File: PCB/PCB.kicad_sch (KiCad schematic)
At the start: 0 parts

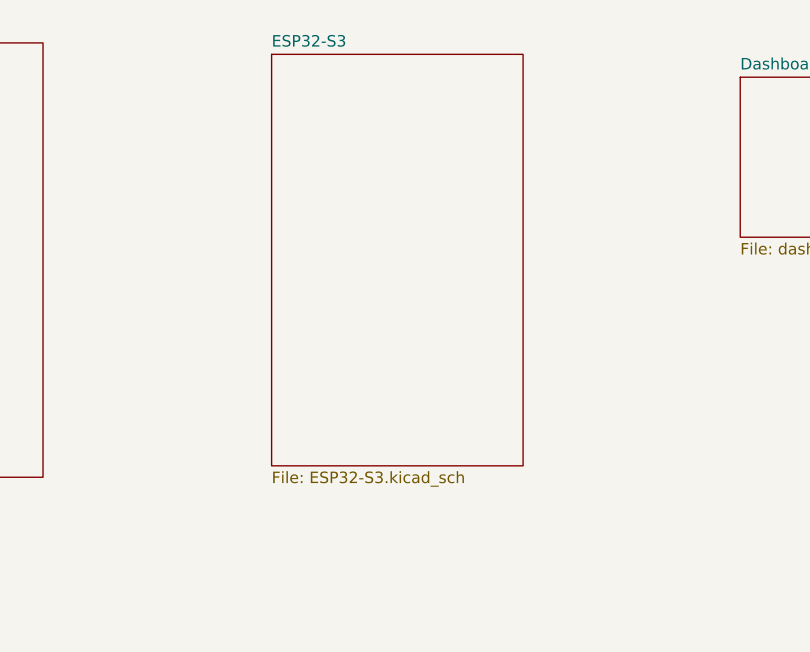
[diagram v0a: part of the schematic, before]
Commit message: [Schem] Added sensors connectors & finished Step down circuit
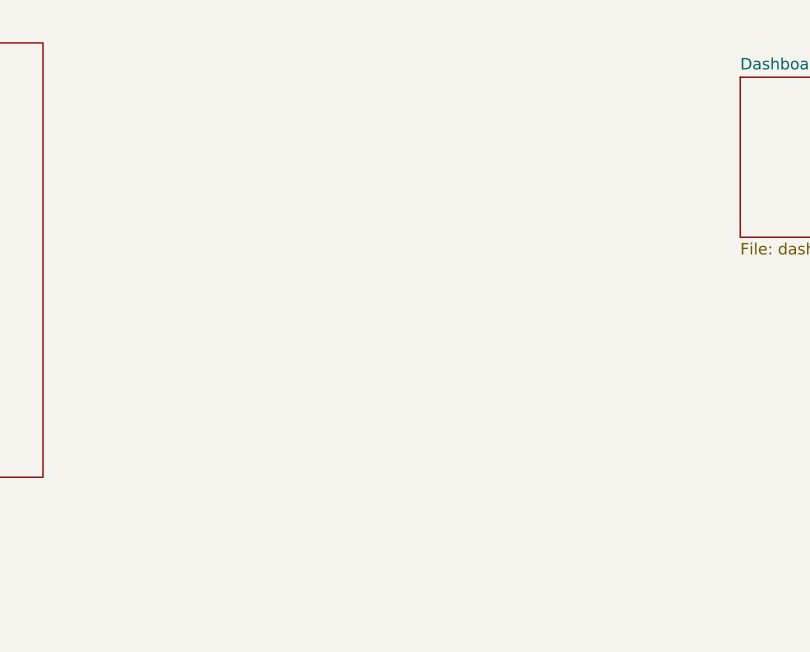
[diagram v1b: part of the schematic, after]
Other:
- removed sheet ESP32-S3
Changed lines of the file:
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@@
-	)
-	(sheet
-		(at 191.77 19.05)
-		(size 27.94 45.72)
-		(exclude_from_sim no)
-		(in_bom yes)
-		(on_board yes)
-		(dnp no)
-		(fields_autoplaced yes)
-		(stroke
-			(width 0.1524)
-			(type solid)
-		)
-		(fill
-			(color 0 0 0 0)
-		)
-		(property "Sheetname" "ESP32-S3"
-			(at 191.77 18.3384 0)
-			(show_name no)
-			(do_not_autoplace no)
-			(effects
-				(font
-					(size 1.27 1.27)
-				)
-				(justify left bottom)
-			)
-		)
-		(property "Sheetfile" "ESP32-S3.kicad_sch"
-			(at 191.77 65.3546 0)
-			(show_name no)
-			(do_not_autoplace no)
-			(effects
-				(font
-					(size 1.27 1.27)
-				)
-				(justify left top)
-			)
-		)
-		(instances
-			(project "PCB"
-				(path "/ce714510-8789-438c-9780-97c7c26e78af"
-					(page "3")
-				)
-			)
-		)
 	)
 	(sheet

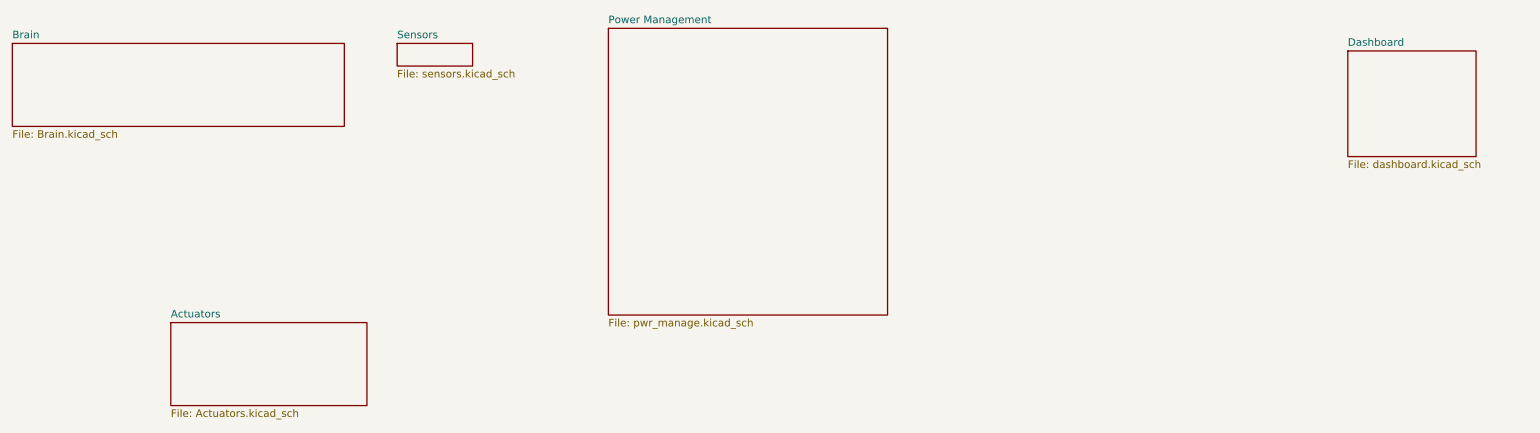
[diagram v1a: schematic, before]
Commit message: [Schem] Finished the Hierarchy Labels of all the pages
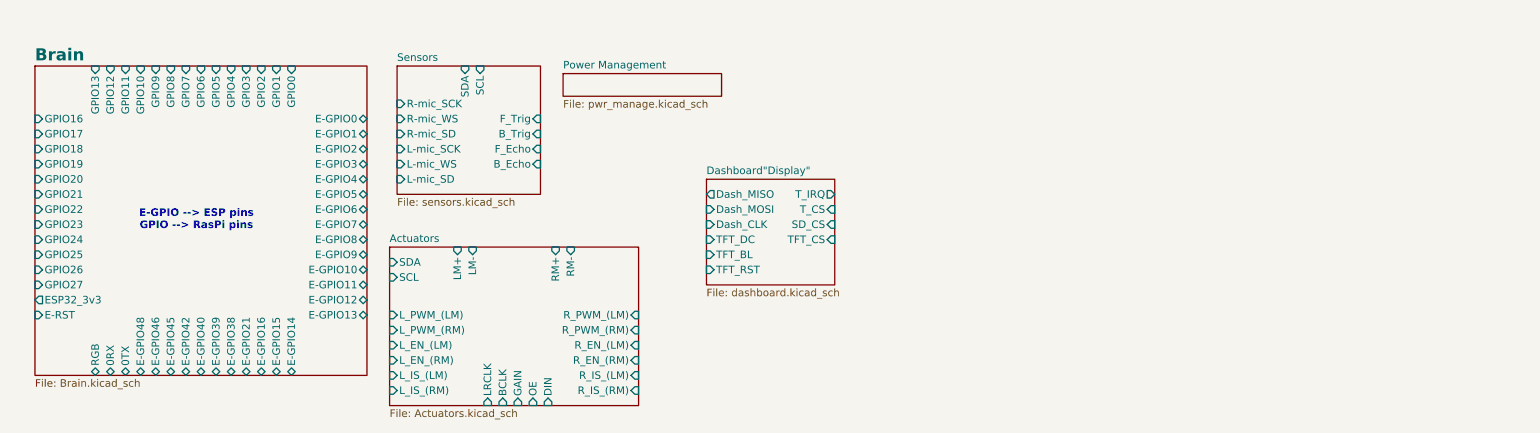
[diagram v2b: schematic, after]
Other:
- sheet Dashboard renamed Dashboard"Display"
- sheet Actuators ports: added BCLK, DIN, GAIN, LM+, LM-, LRCLK, L_EN_(LM), L_EN_(RM), L_IS_(LM), L_IS_(RM), L_PWM_(LM), L_PWM_(RM), OE, RM+, RM-, R_EN_(LM), R_EN_(RM), R_IS_(LM), R_IS_(RM), R_PWM_(LM), R_PWM_(RM), SCL, SDA; removed none
- sheet Brain ports: added 0RX, 0TX, E-GPIO0, E-GPIO1, E-GPIO10, E-GPIO11, E-GPIO12, E-GPIO13, E-GPIO14, E-GPIO15, E-GPIO16, E-GPIO2, E-GPIO21, E-GPIO3, E-GPIO38, E-GPIO39, E-GPIO4, E-GPIO40, E-GPIO42, E-GPIO45, E-GPIO46, E-GPIO48, E-GPIO5, E-GPIO6, E-GPIO7, E-GPIO8, E-GPIO9, E-RST, ESP32_3v3, GPIO0, GPIO1, GPIO10, GPIO11, GPIO12, GPIO13, GPIO16, GPIO17, GPIO18, GPIO19, GPIO2, GPIO20, GPIO21, GPIO22, GPIO23, GPIO24, GPIO25, GPIO26, GPIO27, GPIO3, GPIO4, GPIO5, GPIO6, GPIO7, GPIO8, GPIO9, RGB; removed none
- sheet Dashboard"Display" ports: added Dash_CLK, Dash_MISO, Dash_MOSI, SD_CS, TFT_BL, TFT_CS, TFT_DC, TFT_RST, T_CS, T_IRQ; removed none
- sheet Sensors ports: added B_Echo, B_Trig, F_Echo, F_Trig, L-mic_SCK, L-mic_SD, L-mic_WS, R-mic_SCK, R-mic_SD, R-mic_WS, SCL, SDA; removed none
- note added: "E-GPIO --> ESP pins GPIO --> RasPi pins"

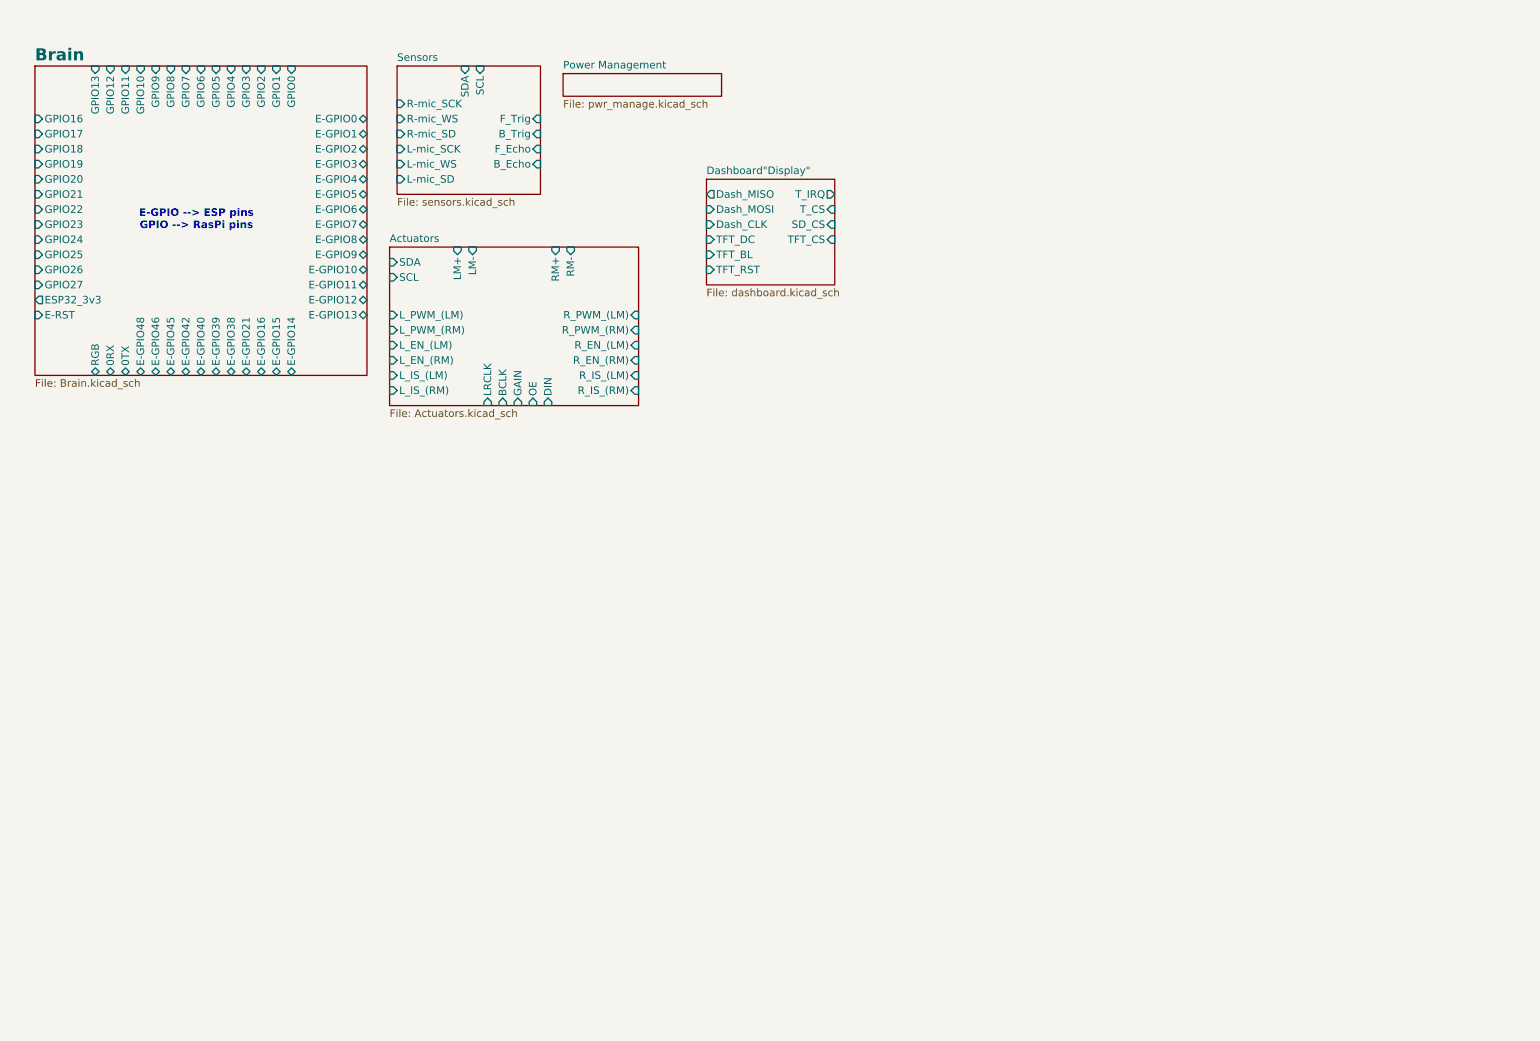
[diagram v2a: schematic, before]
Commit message: [Schem] Added all the net labels and connected the Dashboard screen
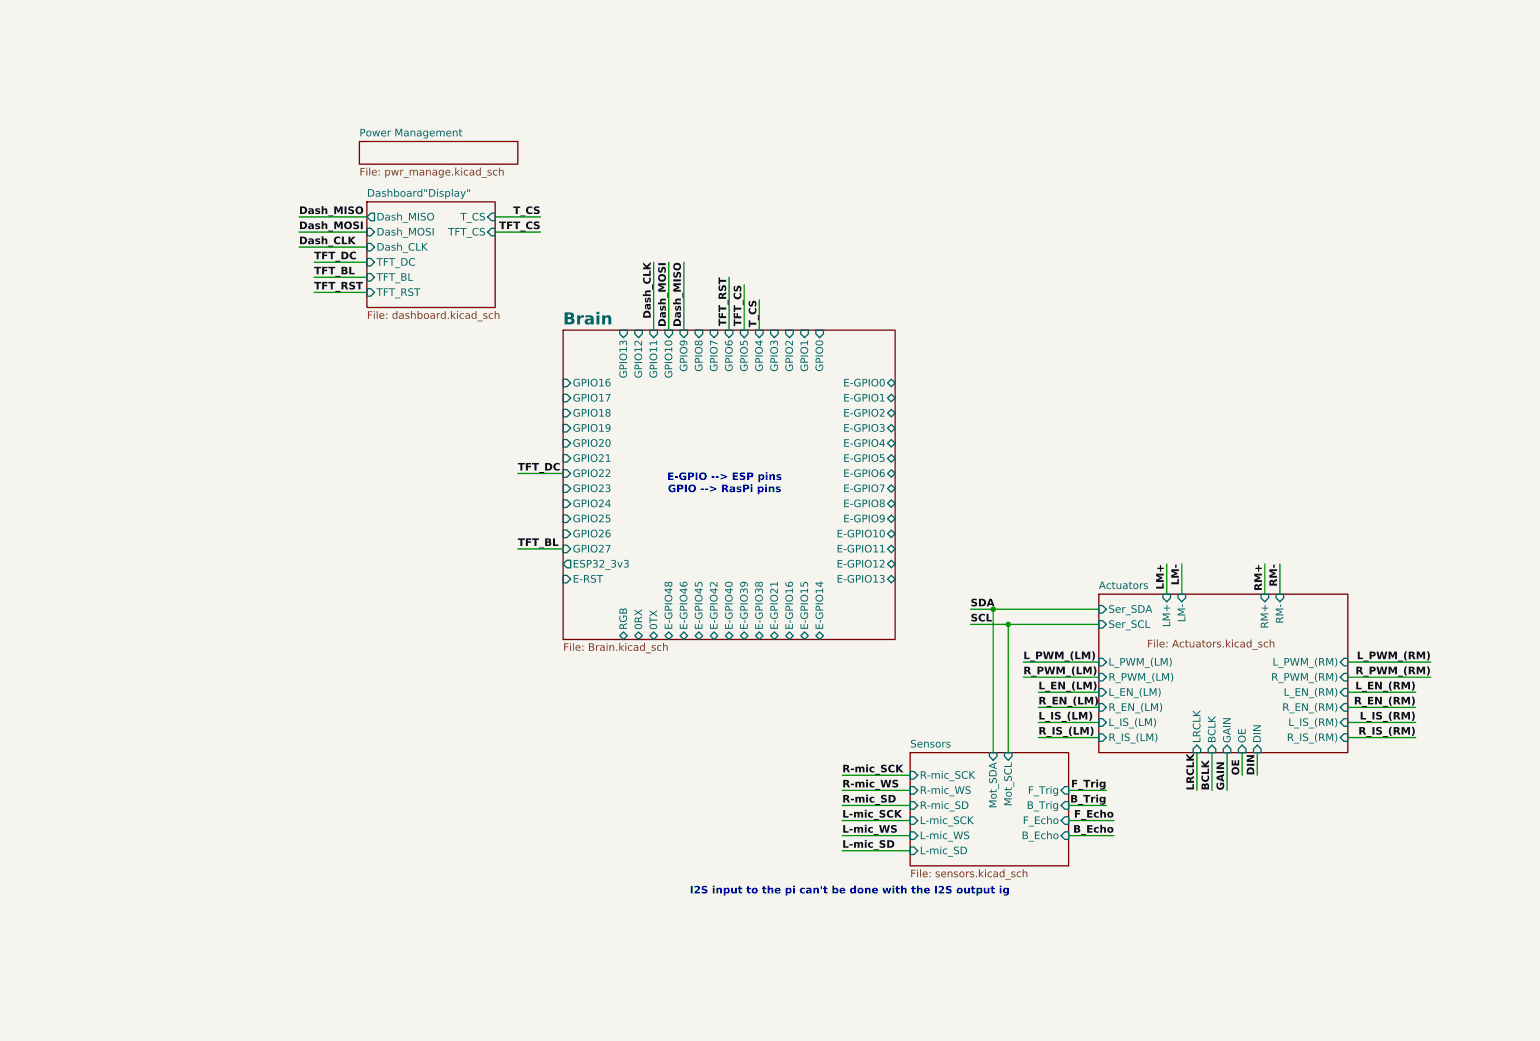
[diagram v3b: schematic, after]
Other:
- sheet Actuators ports: added Ser_SCL, Ser_SDA; removed SCL, SDA
- sheet Dashboard"Display" ports: added none; removed SD_CS, T_IRQ
- sheet Sensors ports: added Mot_SCL, Mot_SDA; removed SCL, SDA
- note added: "I2S input to the pi can't be done with the I2S output ig"

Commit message: [PCB] Assigned all the footprints
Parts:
- added J19: Free_GPIO, Connector_PinHeader_2.54mm:PinHeader_2x11_P2.54mm_Vertical, symbol Connector_Generic:Conn_02x11_Odd_Even
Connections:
- new net E-GPIO0: J19.8 (Pin_8)
- new net E-GPIO16: J19.12 (Pin_12)
- new net E-GPIO21: J19.14 (Pin_14)
- new net E-GPIO3: J19.10 (Pin_10)
- new net E-GPIO38: J19.16 (Pin_16)
- new net E-GPIO39: J19.18 (Pin_18)
- new net E-GPIO40: J19.20 (Pin_20)
- new net ESP32_3v3: J19.22 (Pin_22)
- new net GPIO0: J19.1 (Pin_1)
- new net GPIO1: J19.3 (Pin_3)
- new net GPIO12: J19.13 (Pin_13)
- new net GPIO13: J19.15 (Pin_15)
- new net GPIO16: J19.17 (Pin_17)
- new net GPIO17: J19.19 (Pin_19)
- new net GPIO2: J19.5 (Pin_5)
- new net GPIO23: J19.21 (Pin_21)
- new net GPIO24: J19.2 (Pin_2)
- new net GPIO25: J19.4 (Pin_4)
- new net GPIO26: J19.6 (Pin_6)
- new net GPIO3: J19.7 (Pin_7)
- new net GPIO7: J19.9 (Pin_9)
- new net GPIO8: J19.11 (Pin_11)
- no-connect marks 0 -> 1
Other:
- sheet Actuators ports: added none; removed OE
- sheet Brain ports: added none; removed 0RX, 0TX
- sheet Sensors ports: added mic_SCK, mic_SD, mic_WS; removed L-mic_SCK, L-mic_SD, L-mic_WS, R-mic_SCK, R-mic_SD, R-mic_WS
- note removed: "I2S input to the pi can't be done with the I2S output ig"

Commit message: [PCB] Connected BTs & USB to the ESP
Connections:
- net GPIO0: no longer J19.1 (Pin_1)
- new net RGB: J19.1 (Pin_1)
- no-connect marks 1 -> 3
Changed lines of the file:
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@@
+	)
+	(no_connect
+		(at 165.1 85.09)
+	)
+	(no_connect
+		(at 109.22 115.57)
 	)
 	(no_connect
@@
 	(wire
 		(pts
-			(xy 173.99 85.09) (xy 165.1 85.09)
-		)
-		(stroke
-			(width 0)
-			(type default)
-		)
-	)
-	(wire
-		(pts
 			(xy 105.41 121.92) (xy 97.79 121.92)
 		)
@@
 	(wire
 		(pts
+			(xy 121.92 133.35) (xy 121.92 128.27)
+		)
+		(stroke
+			(width 0)
+			(type default)
+		)
+	)
+	(wire
+		(pts
 			(xy 107.95 142.24) (xy 97.79 142.24)
 		)
@@
 	(wire
 		(pts
-			(xy 78.74 121.92) (xy 85.09 121.92)
+			(xy 80.01 121.92) (xy 85.09 121.92)
 		)
 		(stroke
@@
 		)
 	)
-	(label "E-GPIO0"
-		(at 173.99 85.09 180)
-		(effects
-			(font
-				(size 1.27 1.27)
-			)
-			(justify right bottom)
-		)
-	)
 	(label "E-GPIO16"
 		(at 107.95 134.62 180)
@@
 		)
 	)
+	(label "RGB"
+		(at 121.92 133.35 90)
+		(effects
+			(font
+				(size 1.27 1.27)
+			)
+			(justify left bottom)
+		)
+	)
 	(label "B_Echo"
 		(at 149.86 135.89 90)
@@
 		)
 	)
-	(label "GPIO0"
-		(at 78.74 121.92 0)
+	(label "RGB"
+		(at 80.01 121.92 0)
 		(effects
 			(font
@@
 		(members "02a73960-9642-46b7-a52f-d25257fe207d" "0407dfcd-b798-4dd9-bff4-91ca1fe4759e"
 			"044453e5-acf2-4b60-aee1-132dfd6baebe" "05641111-d300-47e0-9c69-5980f05ecfc0"
-			"0b344c1b-6b4d-4428-9736-f3bae6e344b9" "0be03651-2cdd-486e-949e-fe2203e050f4"
-			"0e9a8393-9e9c-4ee3-a367-d96c46524141" "17b2123f-7b24-45f2-acad-7913332d5c13"
-			"2688dfe6-6bb2-4a56-8bc0-eb036d74d268" "37ad4520-87d4-4f06-935c-abf4ef28a0d1"
-			"399517a1-a159-4530-89a0-9d3a2f8efad6" "3c135e47-ad58-4b68-a3c4-3a1d46d90d8f"
+			"0b344c1b-6b4d-4428-9736-f3bae6e344b9" "0e9a8393-9e9c-4ee3-a367-d96c46524141"
+			"17b2123f-7b24-45f2-acad-7913332d5c13" "2688dfe6-6bb2-4a56-8bc0-eb036d74d268"
+			"37ad4520-87d4-4f06-935c-abf4ef28a0d1" "3c135e47-ad58-4b68-a3c4-3a1d46d90d8f"
 			"42c115a4-ad82-4590-a3ef-25f69765dc21" "4c299918-fc4c-4d6b-8f41-73ed70ef9797"
 			"4f7bcb12-8740-4208-a459-b37e5a953c36" "50545d74-9303-4cd0-a8b1-892d8244d0e3"
 			"527fbd9a-4083-41d5-af5d-3ca3a5675333" "67b2d230-ca5a-4310-99b0-be0492438563"
 			"69146649-3d91-4bca-87cc-5b0691afb6ca" "6f4f81b7-61b4-4f90-a00f-bf691f316eac"
-			"7295a527-7dd4-455f-bdab-ebb540840d40" "781532ae-edf5-4562-9b56-fec3cff04140"
-			"78fe2b96-da3c-432e-b643-996563aa7e2a" "799ed5d8-6991-44f1-91a4-1434dc48aa34"
-			"7a083e45-eeda-4f19-8205-c7463affd60b" "7fffaca1-b23d-47a5-b071-49146a200b05"
-			"82e7289f-0cf3-4a3e-a270-9b70d7d8be67" "8811cf9d-5dd0-4b3e-8464-4c30abdef9b3"
-			"8eaeb52e-fc8a-4624-964e-2d4a9a83f013" "9bc4a975-2c08-411c-92bf-9de1e36174b5"
-			"9dafa989-a928-447c-9f65-864fd41a5f37" "9f244358-bfe9-42e2-bc30-eefbf3fb9059"
-			"a51f9e16-8440-41b0-8985-a8885bc80cff" "b0108336-a320-4871-94c0-adbb3689bdaa"
-			"b07bbe2d-622f-4376-905f-505fb71bc297" "b8a0fa01-0139-4d87-919a-b809db0deeb3"
-			"bb03ce1d-9066-41ca-8766-faa60b079eec" "c6b5b777-27d8-44e8-848c-bf4d541cbdec"
-			"d97e8808-7d86-40ef-b17c-173842b5694b" "e0837900-09b9-4654-bda8-14af42d6503e"
-			"e1fc9d0a-1872-46a1-bdf5-20159dce2788" "e401ba9c-ccbb-4732-81d7-e0599dd79a84"
-			"e946d885-9fab-4821-a016-74bb0347e0e5" "f7b7255e-31a3-4c1b-9115-86465754a995"
-			"f9caf3f0-d619-4e60-a102-301fd7c3a22f" "fcc57ae3-edc1-431d-9edc-702c7b3bd948"
-			"fcf52548-2f27-4861-bba5-0ac34b45eca7"
-		)
-	)
+			"7161c487-c7ba-4fc4-be1a-5b117d4e29a1" "7295a527-7dd4-455f-bdab-ebb540840d40"
+			"781532ae-edf5-4562-9b56-fec3cff04140" "78fe2b96-da3c-432e-b643-996563aa7e2a"
+			"799ed5d8-6991-44f1-91a4-1434dc48aa34" "7a083e45-eeda-4f19-8205-c7463affd60b"
+			"7fffaca1-b23d-47a5-b071-49146a200b05" "82e7289f-0cf3-4a3e-a270-9b70d7d8be67"
+			"8811cf9d-5dd0-4b3e-8464-4c30abdef9b3" "8eaeb52e-fc8a-4624-964e-2d4a9a83f013"
+			"9bc4a975-2c08-411c-92bf-9de1e36174b5" "9dafa989-a928-447c-9f65-864fd41a5f37"
+			"9f244358-bfe9-42e2-bc30-eefbf3fb9059" "a51f9e16-8440-41b0-8985-a8885bc80cff"
+			"b0108336-a320-4871-94c0-adbb3689bdaa" "b07bbe2d-622f-4376-905f-505fb71bc297"
+			"b8a0fa01-0139-4d87-919a-b809db0deeb3" "bb03ce1d-9066-41ca-8766-faa60b079eec"
+			"c6b5b777-27d8-44e8-848c-bf4d541cbdec" "d97e8808-7d86-40ef-b17c-173842b5694b"
+			"e0837900-09b9-4654-bda8-14af42d6503e" "e1fc9d0a-1872-46a1-bdf5-20159dce2788"
+			"e401ba9c-ccbb-4732-81d7-e0599dd79a84" "e946d885-9fab-4821-a016-74bb0347e0e5"
+			"f7b7255e-31a3-4c1b-9115-86465754a995" "f9caf3f0-d619-4e60-a102-301fd7c3a22f"
+			"fcc57ae3-edc1-431d-9edc-702c7b3bd948" "fcf52548-2f27-4861-bba5-0ac34b45eca7"
+		)
+	)

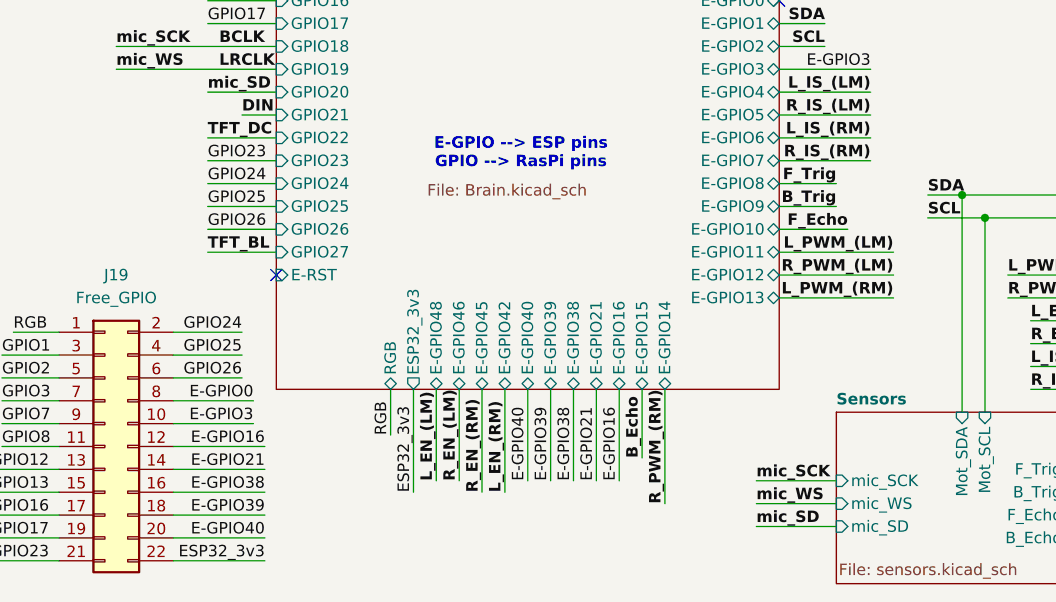
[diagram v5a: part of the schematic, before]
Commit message: [PCB] 95% finished the PCB
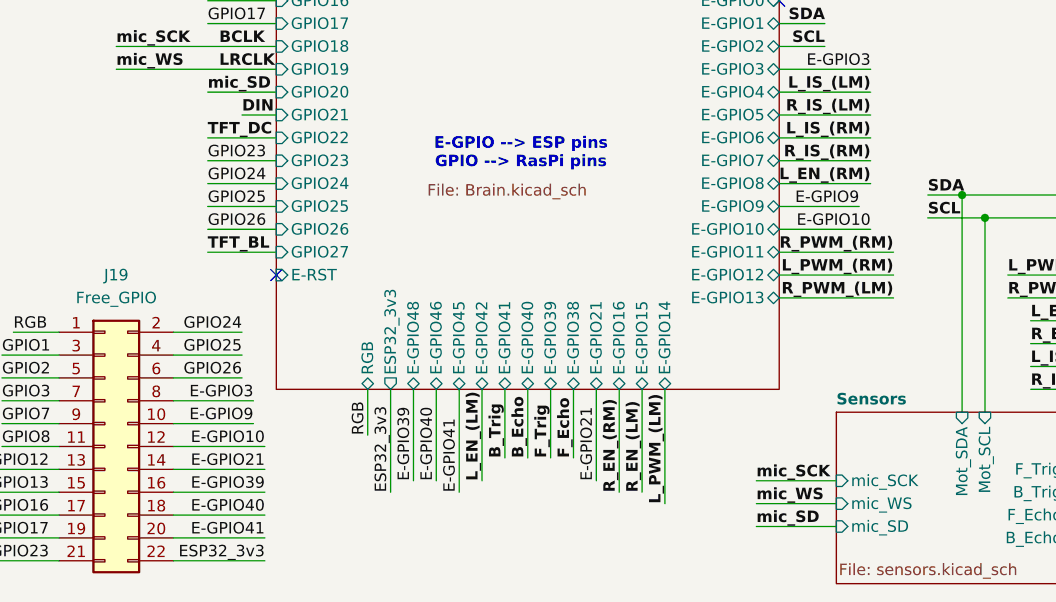
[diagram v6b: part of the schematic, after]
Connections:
- net E-GPIO0 is gone; now on net E-GPIO3: J19.8 (Pin_8)
- net E-GPIO38 is gone; now on net E-GPIO39: J19.16 (Pin_16)
- net E-GPIO3: no longer J19.10 (Pin_10)
- net E-GPIO39: no longer J19.18 (Pin_18)
- net E-GPIO40: now also J19.18 (Pin_18); no longer J19.20 (Pin_20)
- net E-GPIO16 renamed E-GPIO10
- new net E-GPIO41: J19.20 (Pin_20)
- new net E-GPIO9: J19.10 (Pin_10)
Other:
- sheet Brain ports: added E-GPIO41; removed none
